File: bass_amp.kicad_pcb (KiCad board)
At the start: 2 copper layers, 70.9 x 25.9 mm, 20 parts, among them J1 AudioJack3, J2 PICKUP_SIGNAL, J3 PICKUP_GND, J4 PWR, J5 GND, Q1 BC547, Q2 BC547, SW1 SW_Push_DPDT

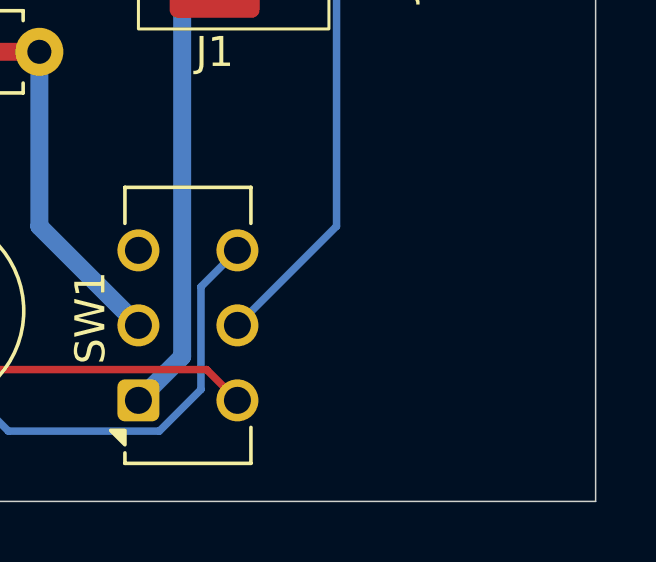
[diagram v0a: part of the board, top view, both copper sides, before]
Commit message: Add a custom Frieren logo
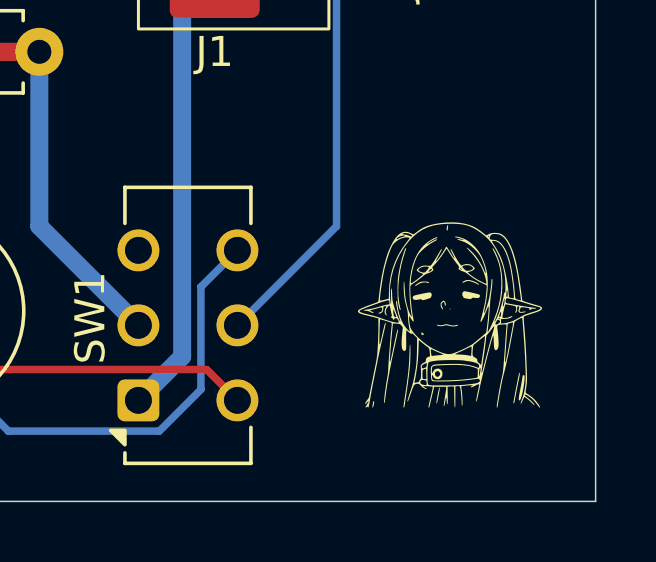
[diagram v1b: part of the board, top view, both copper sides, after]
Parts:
- added G***: LOGO, Custom_Connectors:Frieren, F.Cu at (182.9, 80.8)

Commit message: Fill empty PCB zones with GND
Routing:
- net GND: vias 0 -> 2
- added copper zone on B.Cu, net GND
- added copper zone on F.Cu, net GND
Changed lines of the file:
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@@
+		(net 8)
+	)
+	(via
+		(at 183.642 69.596)
+		(size 0.6)
+		(drill 0.3)
+		(layers "F.Cu" "B.Cu")
+		(net 8)
+	)
+	(via
+		(at 175.006 69.85)
+		(size 0.6)
+		(drill 0.3)
+		(layers "F.Cu" "B.Cu")
 		(net 8)
 	)
@@
 		(net 14)
 	)
+	(zone
+		(net 8)
+		(net_name "GND")
+		(layers "F.Cu" "B.Cu")
+		(hatch edge 0.5)
+		(connect_pads
+			(clearance 0.5)
+		)
+		(min_thickness 0.25)
+		(filled_areas_thickness no)
+		(fill yes
+			(thermal_gap 0.5)
+			(thermal_bridge_width 0.5)
+		)
+		(polygon
+			(pts
+				(xy 116.84 60.96) (xy 116.84 86.868) (xy 187.706 86.868) (xy 187.706 60.96)
+			)
+		)
+	)
 	(embedded_fonts no)

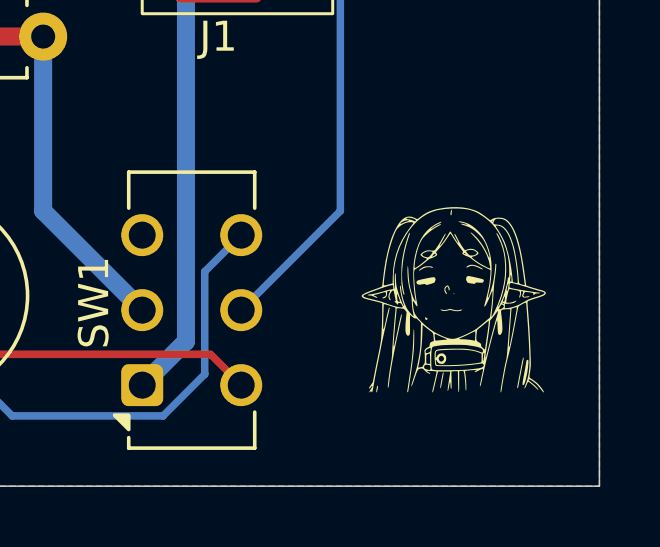
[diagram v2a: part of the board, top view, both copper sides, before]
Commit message: Add a separate library for logos
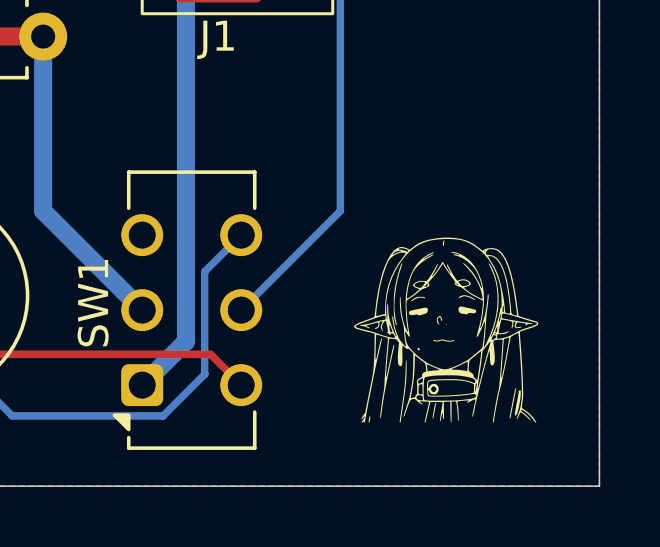
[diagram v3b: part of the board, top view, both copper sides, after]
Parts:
- removed the G*** at (182.9, 80.8)
- added G***: LOGO, Custom_Logos:Frieren, F.Cu at (182.6, 81.8)
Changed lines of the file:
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@@
 		)
 	)
-	(footprint "Custom_Connectors:Frieren"
+	(footprint "Custom_Logos:Frieren"
 		(layer "F.Cu")
-		(at 182.88 80.772)
+		(at 182.626 81.788)
 		(property "Reference" "G***"
 			(at 0 0 0)

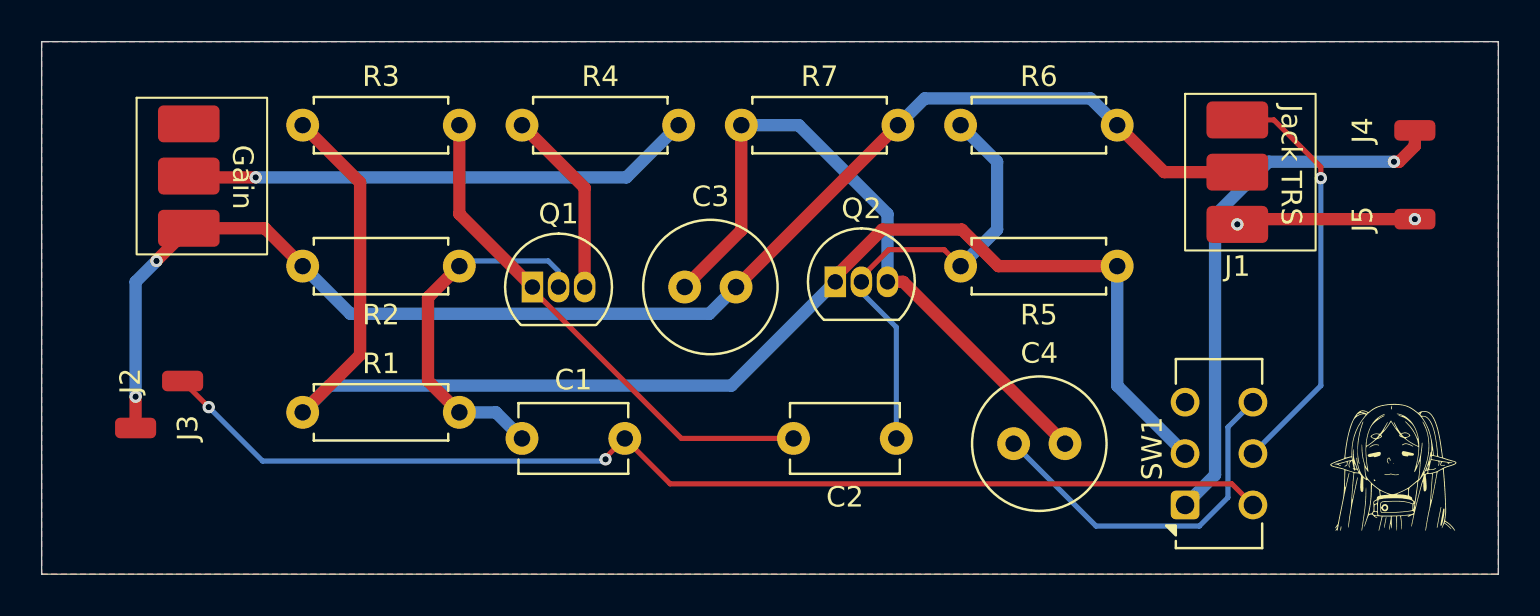
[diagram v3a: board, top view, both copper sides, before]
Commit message: Add mounting holes to the PCB
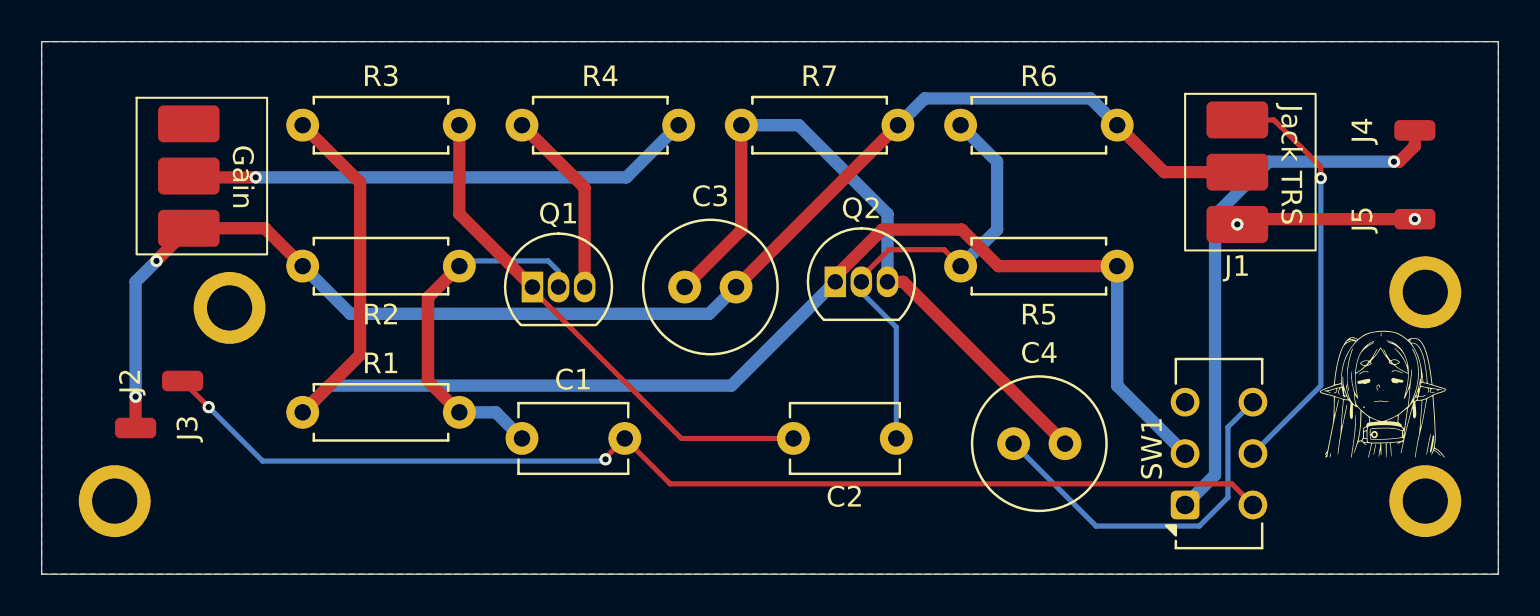
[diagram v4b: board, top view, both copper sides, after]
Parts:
- added REF**: MountingHole_2.2mm_M2_ISO7380_Pad, MountingHole:MountingHole_2.2mm_M2_ISO7380_Pad, F.Cu at (120.4, 83.3)
- added REF**: MountingHole_2.2mm_M2_ISO7380_Pad, MountingHole:MountingHole_2.2mm_M2_ISO7380_Pad, F.Cu at (184.2, 73.2)
- added REF**: MountingHole_2.2mm_M2_ISO7380_Pad, MountingHole:MountingHole_2.2mm_M2_ISO7380_Pad, F.Cu at (126.0, 73.9)
- added REF**: MountingHole_2.2mm_M2_ISO7380_Pad, MountingHole:MountingHole_2.2mm_M2_ISO7380_Pad, F.Cu at (184.2, 83.3)
- moved G*** 3.59 mm to (182.1, 78.2)

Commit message: Fix GND connections and rewire the board's GND traces
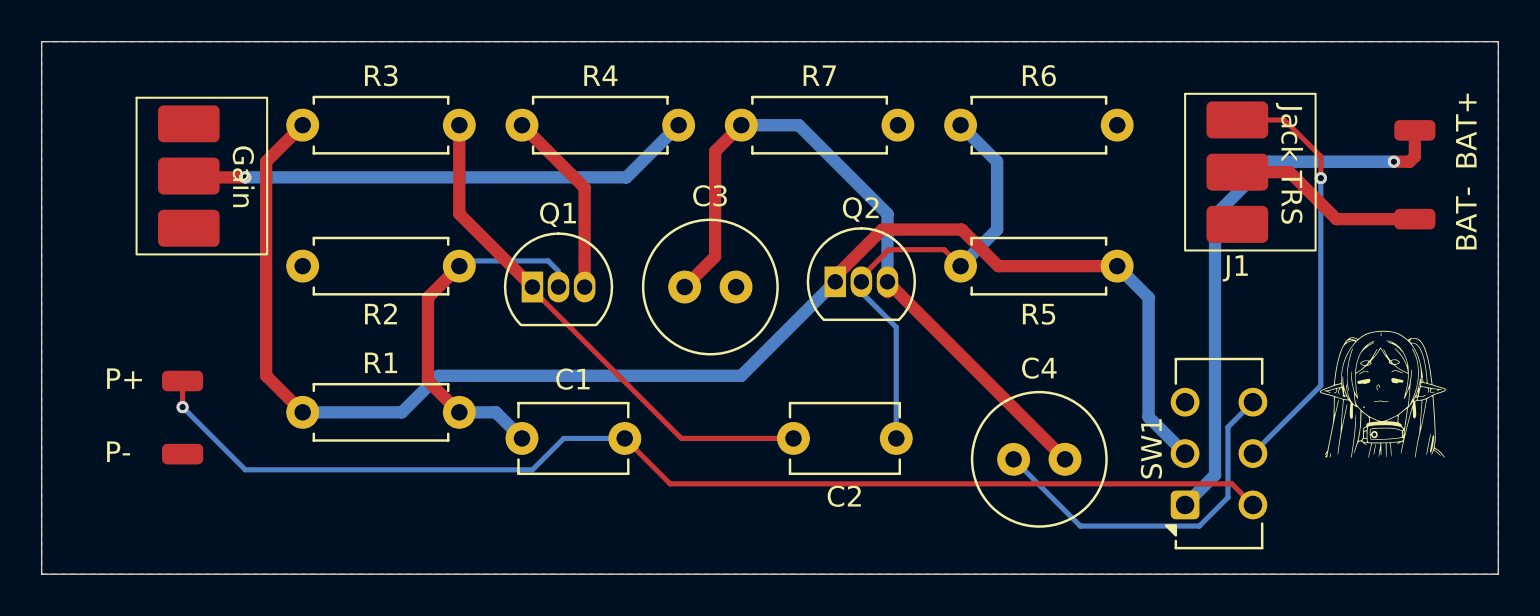
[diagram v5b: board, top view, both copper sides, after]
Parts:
- removed REF** (x4): MountingHole_2.2mm_M2_ISO7380_Pad, MountingHole:MountingHole_2.2mm_M2_ISO7380_Pad
- J4: value PWR -> BAT+
- J5: value GND -> BAT-
- moved J3 2.62 mm to (123.7, 81.0)
- moved C4 0.76 mm to (164.1, 81.3)
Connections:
- C3 pad 2: JACK_R -> GND
- J1 pad R: JACK_R -> -BATT
- J3 pad 1: JACK_R -> GND
- J5 pad 1: GND -> -BATT
- R2 pad 2: JACK_R -> GND
- R6 pad 2: JACK_R -> GND
- R7 pad 2: JACK_R -> GND
- RV1 pad 3: JACK_R -> GND
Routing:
- net JACK_R: track 69.5 -> 0.00 mm, vias 2 -> 0
- net -BATT: track 0.00 -> 9.58 mm
- net GND: track 8.74 -> 0.49 mm, vias 2 -> 0
- net SIGNAL_IN: track 55.5 -> 56.6 mm, vias 2 -> 1
- net VCC_EN: track 71.0 -> 70.1 mm
- net Net-(Q2-E): track 33.1 -> 33.9 mm
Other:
- board text added: "P+"
- board text added: "P-"
